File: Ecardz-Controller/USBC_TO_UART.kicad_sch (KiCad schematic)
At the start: 13 parts, among them J8 Conn_01x04, U4 CP2110-F02-GM1

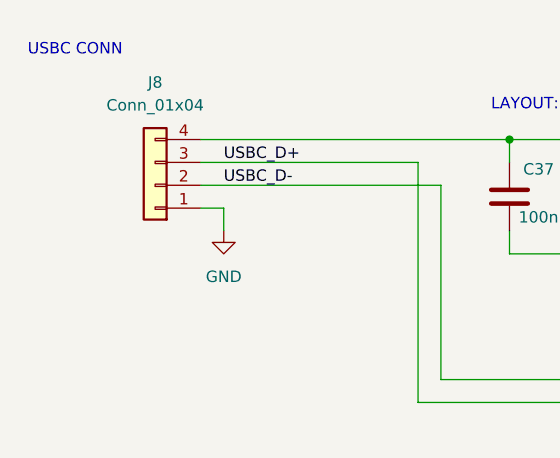
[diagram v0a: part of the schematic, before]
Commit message: moved headers to bottom of board, made J3 DNP
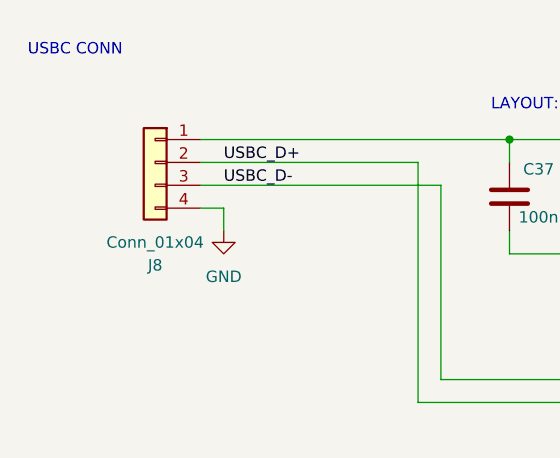
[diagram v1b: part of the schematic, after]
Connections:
- net 5V_USBC: now also J8.1 (Pin_1); no longer J8.4 (Pin_4)
- net GND: now also J8.4 (Pin_4); no longer J8.1 (Pin_1)
- net USBC_D+: now also J8.2 (Pin_2); no longer J8.3 (Pin_3)
- net USBC_D-: now also J8.3 (Pin_3); no longer J8.2 (Pin_2)
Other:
- moved on the sheet: J8
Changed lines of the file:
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@@
 	(paper "A4")
+	(junction
+		(at 77.47 29.21)
+		(diameter 0)
+		(color 0 0 0 0)
+	)
 	(junction
 		(at 114.3 29.21)
@@
 		(color 0 0 0 0)
 	)
-	(junction
-		(at 77.47 29.21)
-		(diameter 0)
-		(color 0 0 0 0)
-	)
 	(no_connect
 		(at 129.54 81.28)
@@
 	(wire
 		(pts
+			(xy 43.18 34.29) (xy 69.85 34.29)
+		)
+		(stroke
+			(width 0)
+			(type default)
+		)
+	)
+	(wire
+		(pts
 			(xy 116.84 105.41) (xy 116.84 101.6)
 		)
@@
 	(wire
 		(pts
+			(xy 170.18 41.91) (xy 170.18 49.53)
+		)
+		(stroke
+			(width 0)
+			(type default)
+		)
+	)
+	(wire
+		(pts
 			(xy 43.18 31.75) (xy 67.31 31.75)
 		)
@@
 	(wire
 		(pts
-			(xy 170.18 41.91) (xy 170.18 49.53)
-		)
-		(stroke
-			(width 0)
-			(type default)
-		)
-	)
-	(wire
-		(pts
 			(xy 77.47 39.37) (xy 77.47 41.91)
 		)
@@
 	(wire
 		(pts
+			(xy 69.85 55.88) (xy 104.14 55.88)
+		)
+		(stroke
+			(width 0)
+			(type default)
+		)
+	)
+	(wire
+		(pts
 			(xy 43.18 36.83) (xy 45.72 36.83)
 		)
@@
 	(wire
 		(pts
-			(xy 69.85 55.88) (xy 104.14 55.88)
-		)
-		(stroke
-			(width 0)
-			(type default)
-		)
-	)
-	(wire
-		(pts
 			(xy 140.97 73.66) (xy 140.97 77.47)
 		)
@@
 		(pts
 			(xy 182.88 41.91) (xy 182.88 49.53)
-		)
-		(stroke
-			(width 0)
-			(type default)
-		)
-	)
-	(wire
-		(pts
-			(xy 43.18 34.29) (xy 69.85 34.29)
 		)
 		(stroke
@@
 	(label "USBC_D+"
 		(at 91.44 58.42 0)
-		(fields_autoplaced yes)
 		(effects
 			(font
@@
 	(label "VDD"
 		(at 137.16 31.75 0)
-		(fields_autoplaced yes)
 		(effects
 			(font
@@
 	(label "USBC_D-"
 		(at 91.44 55.88 0)
-		(fields_autoplaced yes)
 		(effects
 			(font
@@
 	(label "USBC_D-"
 		(at 45.72 34.29 0)
-		(fields_autoplaced yes)
 		(effects
 			(font
@@
 	(label "USBC_D+"
 		(at 45.72 31.75 0)
-		(fields_autoplaced yes)
 		(effects
 			(font
@@
 		(shape input)
 		(at 149.86 43.18 0)
-		(fields_autoplaced yes)
 		(effects
 			(font
@@
 		(shape input)
 		(at 149.86 40.64 0)
-		(fields_autoplaced yes)
 		(effects
 			(font
@@
 		(shape input)
 		(at 119.38 29.21 0)
-		(fields_autoplaced yes)
 		(effects
 			(font
@@
 	(symbol
 		(lib_id "Connector_Generic:Conn_01x04")
-		(at 38.1 34.29 180)
+		(at 38.1 31.75 0)
+		(mirror y)
 		(unit 1)
 		(exclude_from_sim no)
@@
 		(on_board yes)
 		(dnp no)
-		(fields_autoplaced yes)
 		(property "Reference" "J8"
-			(at 38.1 22.86 0)
+			(at 38.1 43.18 0)
 			(effects
 				(font
@@
 		)
 		(property "Value" "Conn_01x04"
-			(at 38.1 25.4 0)
+			(at 38.1 40.64 0)
 			(effects
 				(font
@@
 		)
 		(property "Footprint" "Connector_PinHeader_2.54mm:PinHeader_1x04_P2.54mm_Horizontal"
-			(at 38.1 34.29 0)
+			(at 38.1 31.75 0)
 			(effects
 				(font
@@
 		)
 		(property "Datasheet" ""
-			(at 38.1 34.29 0)
+			(at 38.1 31.75 0)
 			(effects
 				(font
@@
 		)
 		(property "Description" "Generic connector, single row, 01x04, script generated (kicad-library-utils/schlib/autogen/connector/)"
-			(at 38.1 34.29 0)
+			(at 38.1 31.75 0)
 			(effects
 				(font
@@
 		)
 		(property "Part Number" "61300411121"
-			(at 38.1 34.29 0)
-			(effects
-				(font
+			(at 38.1 31.75 0)
+			(effects
+				(font
